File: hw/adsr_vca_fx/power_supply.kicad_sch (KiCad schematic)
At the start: 3 parts, among them J1 Conn_01x03, J2 Conn_02x02_Odd_Even, J3 Conn_02x02_Odd_Even

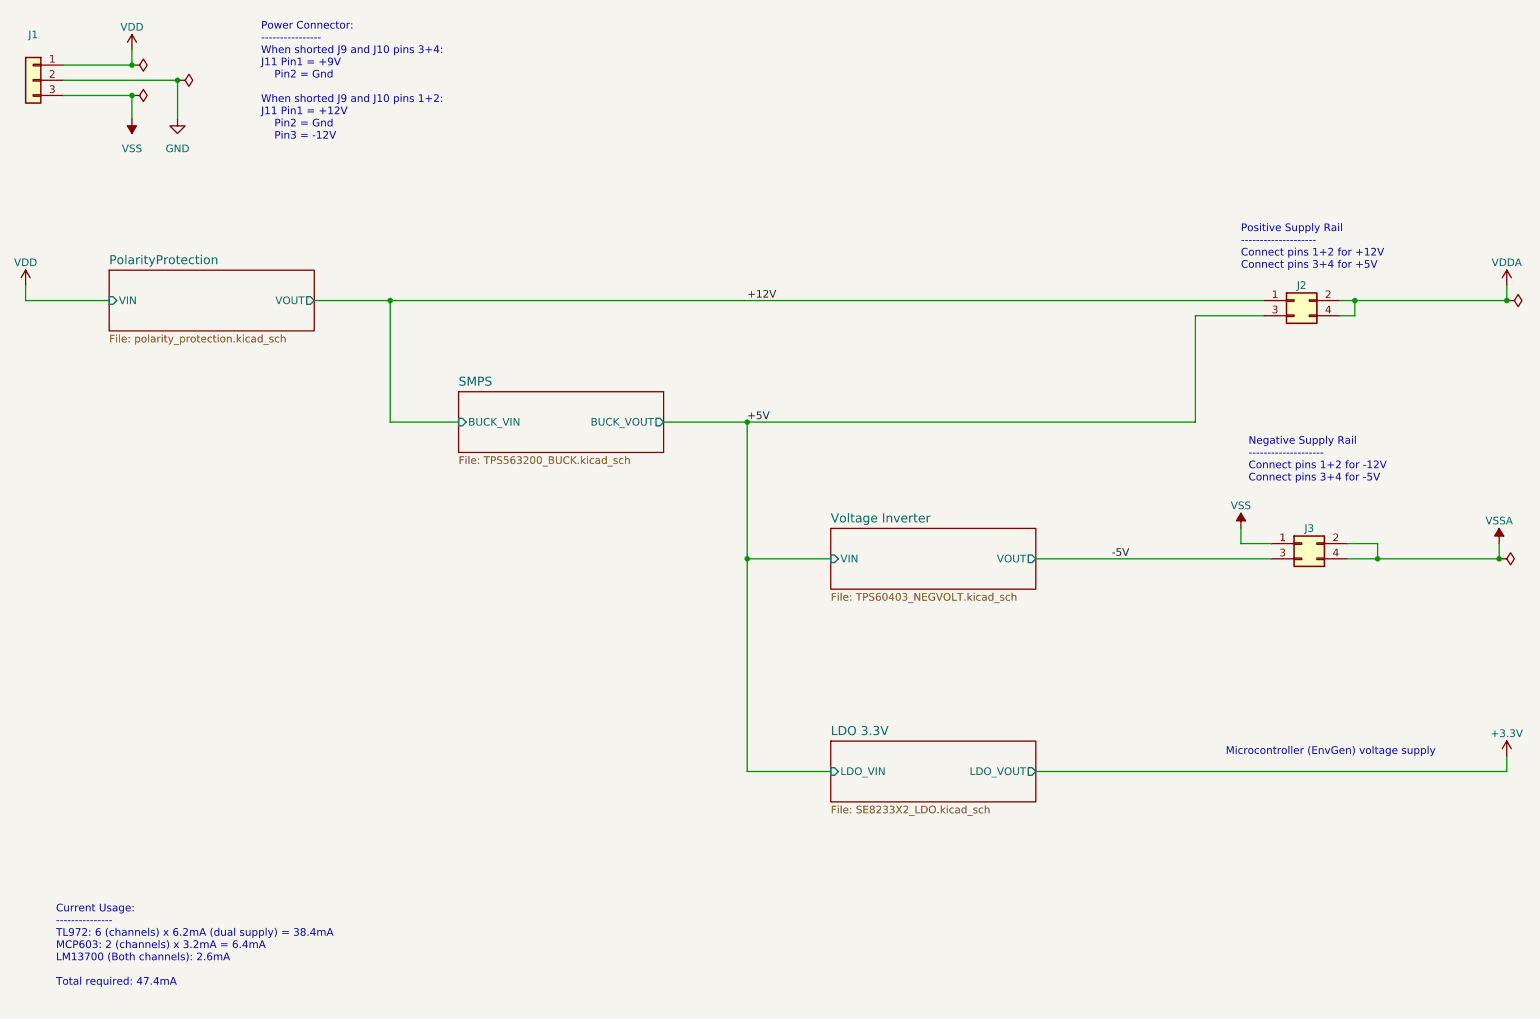
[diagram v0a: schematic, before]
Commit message: modified design into normal/inverted envlope
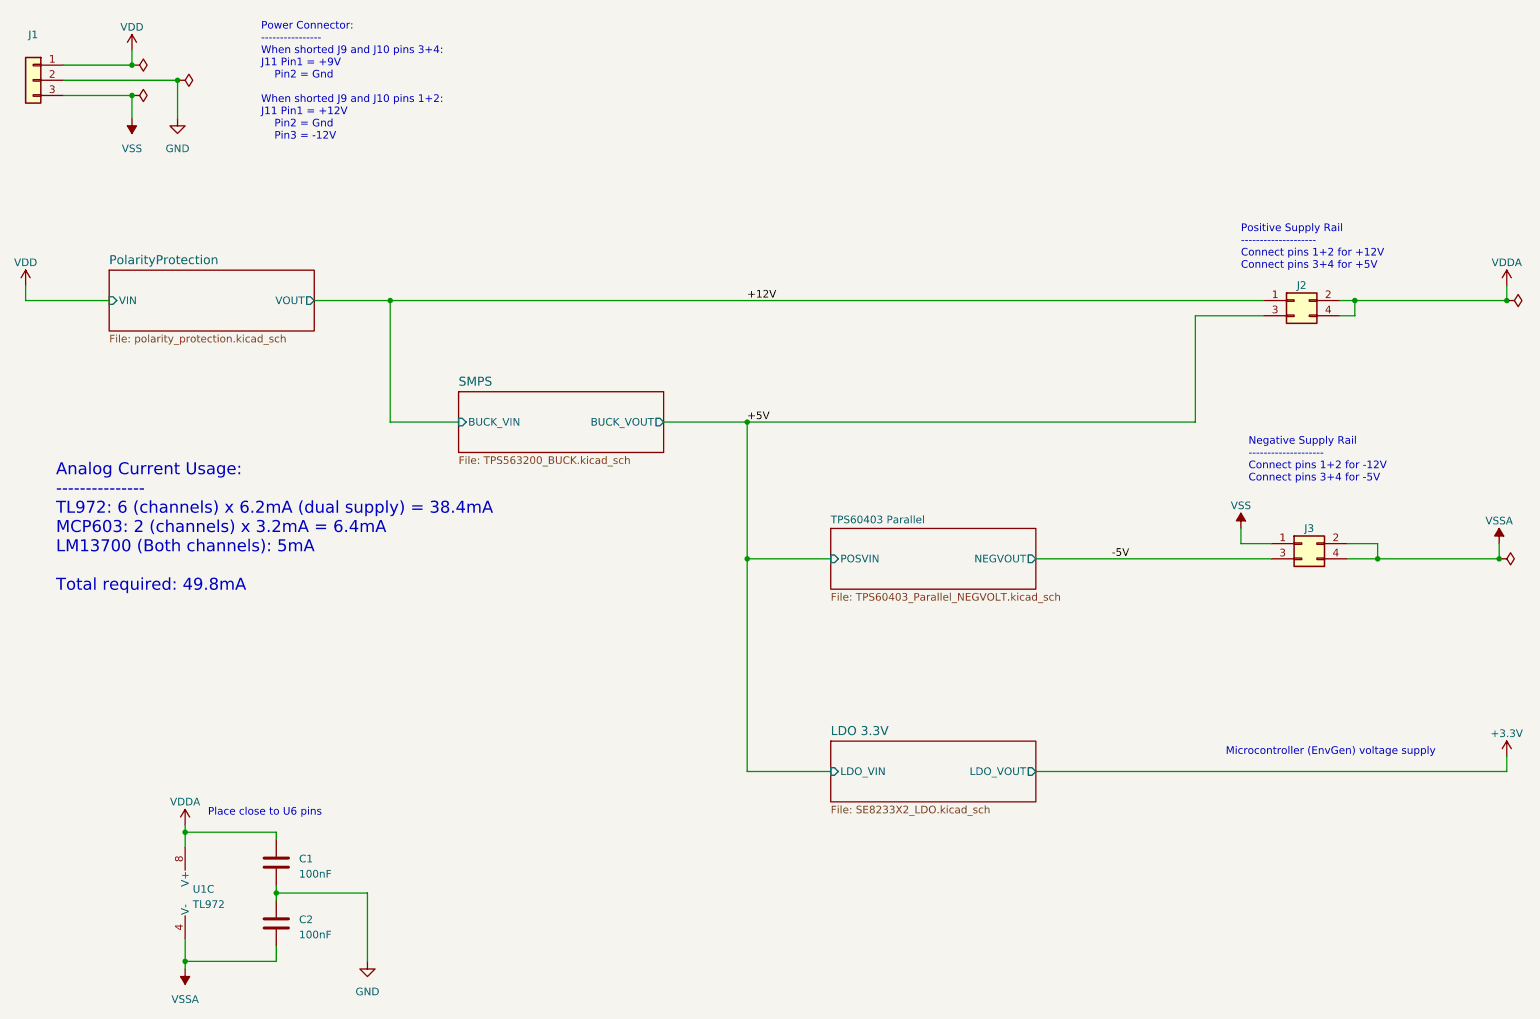
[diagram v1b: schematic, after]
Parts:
- added C1, C2: 100nF, Capacitor_SMD:C_0805_2012Metric_Pad1.18x1.45mm_HandSolder, symbol Device:C
- added U1: TL972, Package_SO:SOIC-8_3.9x4.9mm_P1.27mm, symbol Amplifier_Operational:TL072
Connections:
- net GND: now also C1.2, C2.1
- net VDDA: now also C1.1, U1.8 (V+)
- net VSSA: now also C2.2, U1.4 (V-)
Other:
- removed sheet Voltage Inverter
- added sheet TPS60403 Parallel  (TPS60403_Parallel_NEGVOLT.kicad_sch)
- note added: "Analog Current Usage: --------------- TL972: 6 (channels) x 6.2mA (dual supply) = 38.4mA MCP603: 2 (channels) x 3.2mA = 6.4mA LM13700 (Both channels): 5mA Total required: 49.8mA"
- note added: "Place close to U6 pins"
- note removed: "Current Usage: --------------- TL972: 6 (channels) x 6.2mA (dual supply) = 38.4mA MCP603: 2 (channels) x 3.2mA = 6.4mA LM13700 (Both channels): 2.6mA Total required: 47.4mA"

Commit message: first draft layout
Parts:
- J2, J3: footprint Connector_PinHeader_2.54mm:PinHeader_1x02_P2.54mm_Vertical -> Connector_PinHeader_2.54mm:PinHeader_2x02_P2.54mm_Vertical
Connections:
- net -5V: now also J3.1 (Pin_1); no longer J3.3 (Pin_3)
- net VSS: now also J3.3 (Pin_3); no longer J3.1 (Pin_1)
- net +12V renamed PolarityProtection/VOUT
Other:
- note added: "Place close to U1 pins"
- note removed: "Place close to U6 pins"

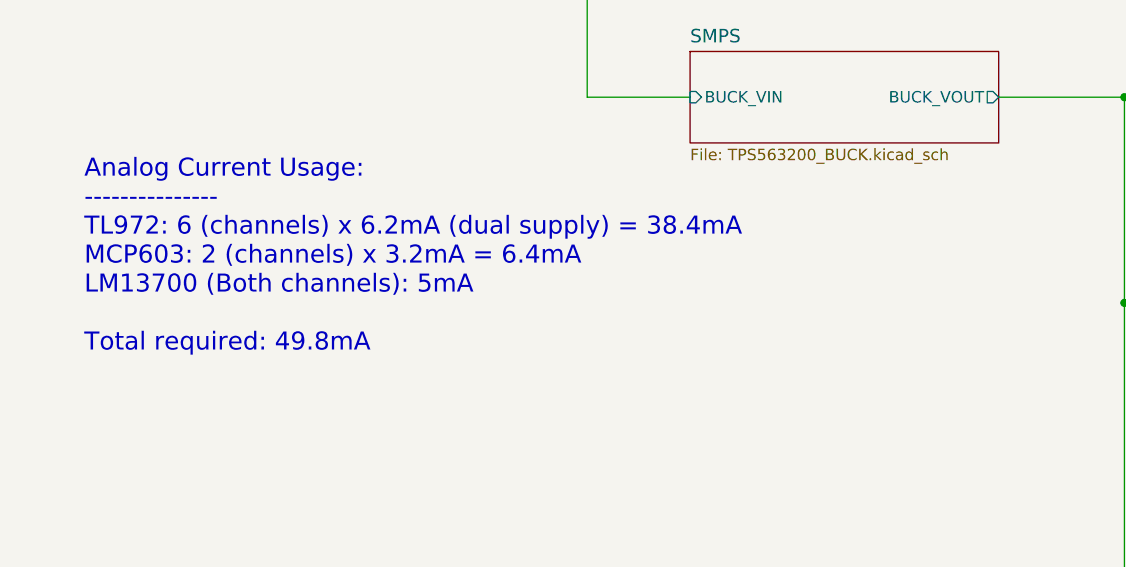
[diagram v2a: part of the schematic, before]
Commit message: updated layout
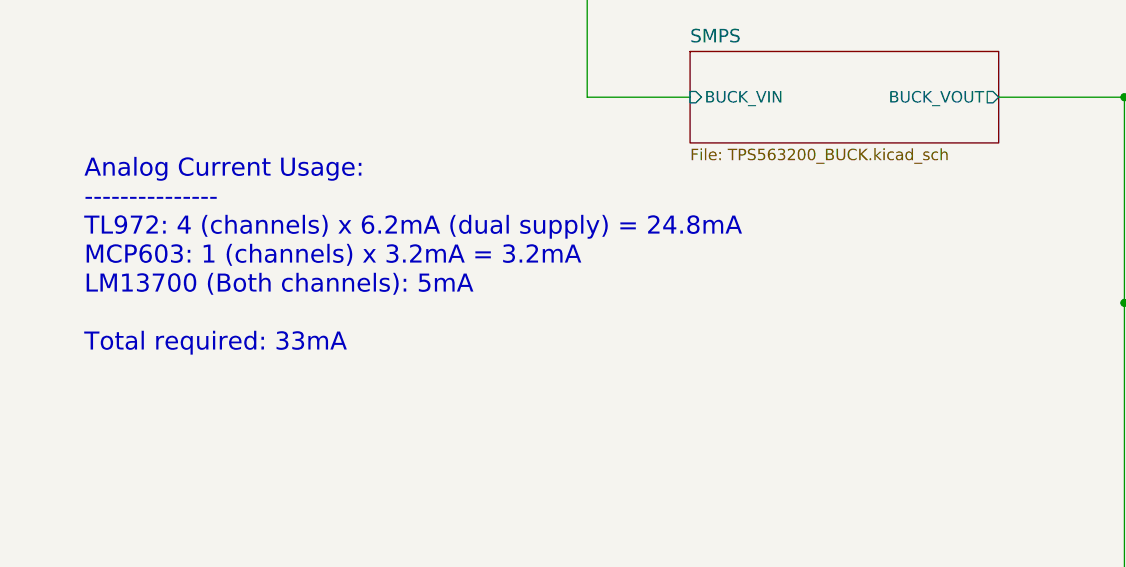
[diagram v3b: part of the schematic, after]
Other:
- note added: "Analog Current Usage: --------------- TL972: 4 (channels) x 6.2mA (dual supply) = 24.8mA MCP603: 1 (channels) x 3.2mA = 3.2mA LM13700 (Both channels): 5mA Total required: 33mA"
- note removed: "Analog Current Usage: --------------- TL972: 6 (channels) x 6.2mA (dual supply) = 38.4mA MCP603: 2 (channels) x 3.2mA = 6.4mA LM13700 (Both channels): 5mA Total required: 49.8mA"
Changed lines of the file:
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@@
-    (stroke (width 0) (type default))
-  )
-  (wire (pts (xy 83.82 69.85) (xy 83.82 90.17))
     (stroke (width 0) (type default))
   )
@@
   )
   (wire (pts (xy 48.26 33.02) (xy 48.26 39.37))
+    (stroke (width 0) (type default))
+  )
+  (wire (pts (xy 83.82 69.85) (xy 83.82 90.17))
     (stroke (width 0) (type default))
   )
@@
     (effects (font (size 1.27 1.27)) (justify left bottom))
   )
-  (text "Analog Current Usage:\n---------------\nTL972: 6 (channels) x 6.2mA (dual supply) = 38.4mA\nMCP603: 2 (channels) x 3.2mA = 6.4mA\nLM13700 (Both channels): 5mA\n\nTotal required: 49.8mA\n\n"
+  (text "Analog Current Usage:\n---------------\nTL972: 4 (channels) x 6.2mA (dual supply) = 24.8mA\nMCP603: 1 (channels) x 3.2mA = 3.2mA\nLM13700 (Both channels): 5mA\n\nTotal required: 33mA\n\n"
     (at 27.94 121.92 0)
     (effects (font (size 2 2)) (justify left bottom))

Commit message: completed layout
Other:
- moved on the sheet: J2, J3

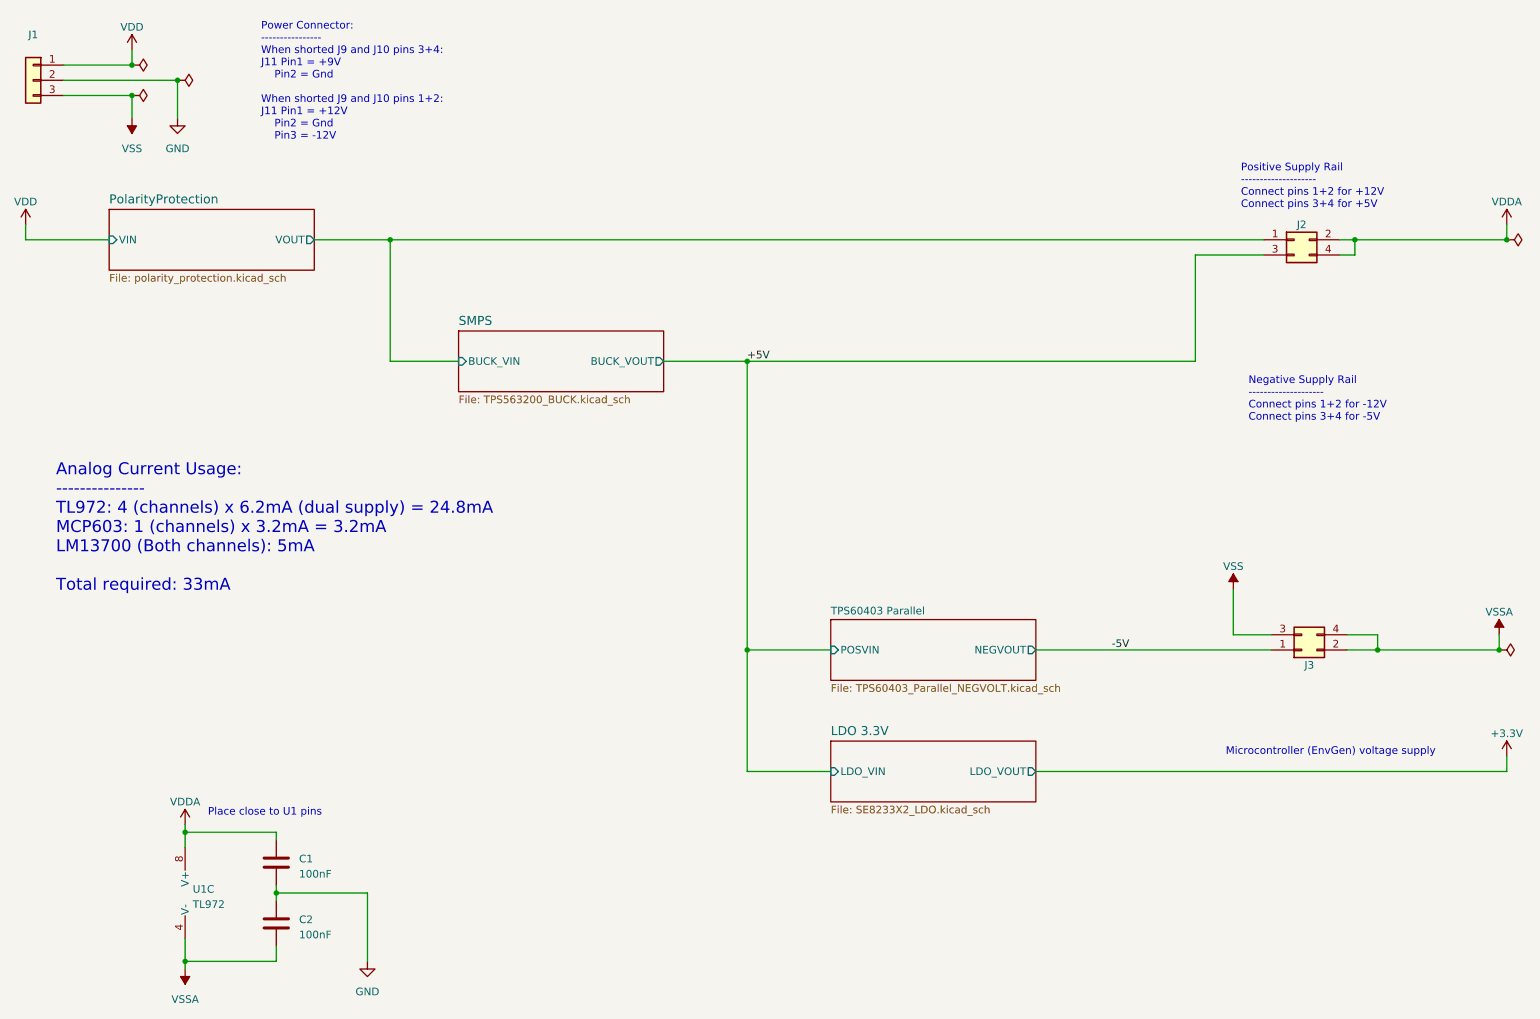
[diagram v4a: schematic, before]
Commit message: RevB; simplified power supply
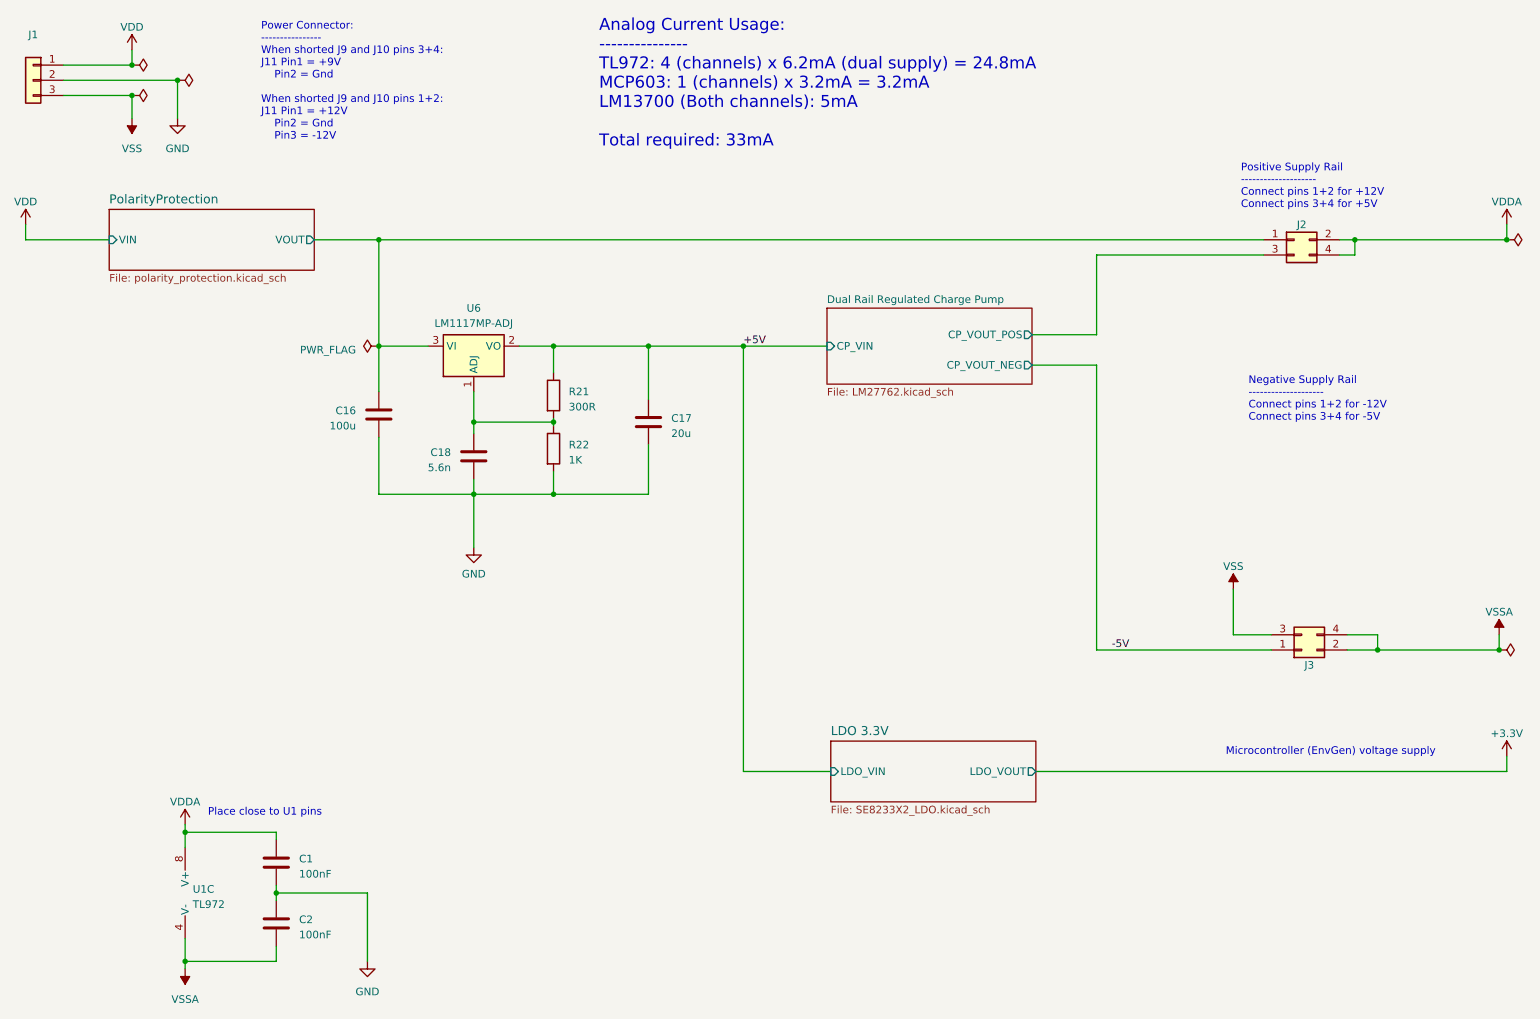
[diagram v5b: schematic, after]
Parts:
- added C16: 100u, Capacitor_SMD:C_Elec_8x5.4, symbol Device:C
- added C17: 20u, Capacitor_SMD:C_Elec_5x5.4, symbol Device:C
- added C18: 5.6n, Capacitor_SMD:C_0805_2012Metric_Pad1.18x1.45mm_HandSolder, symbol Device:C
- added R21: 300R, Resistor_SMD:R_0805_2012Metric_Pad1.20x1.40mm_HandSolder, symbol Device:R
- added R22: 1K, Resistor_SMD:R_0805_2012Metric_Pad1.20x1.40mm_HandSolder, symbol Device:R
- added U6: LM1117MP-ADJ, Package_TO_SOT_SMD:SOT-223-3_TabPin2, symbol Regulator_Linear:LM1117MP-ADJ
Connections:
- net +5V: now also C17.1, R21.1, U6.2 (VO); no longer J2.3 (Pin_3)
- net GND: now also C16.2, C17.2, C18.2, R22.2
- net PolarityProtection/VOUT: now also C16.1, U6.3 (VI)
- new net: C18.1, R21.2, R22.1, U6.1 (ADJ)
- new net Dual Rail Regulated Charge Pump/CP_VOUT_POS: J2.3 (Pin_3)
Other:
- removed sheet SMPS
- removed sheet TPS60403 Parallel 
- added sheet Dual Rail Regulated Charge Pump (LM27762.kicad_sch)
